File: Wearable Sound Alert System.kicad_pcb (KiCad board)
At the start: 2 copper layers, 87 parts, among them J1 ST-LINK Connector, J8 USB4125-GF-A_REVA2, J9 Extra GPIO Header, SW1 SW_Push, U1 STM32F767ZIT6, U2 TPS63020DSJR, U3 MAX17055ETB+T, U4 2.8_240x320_touch_sd_spi, U6 TPS63020DSJR, U7 BQ21040DBVR

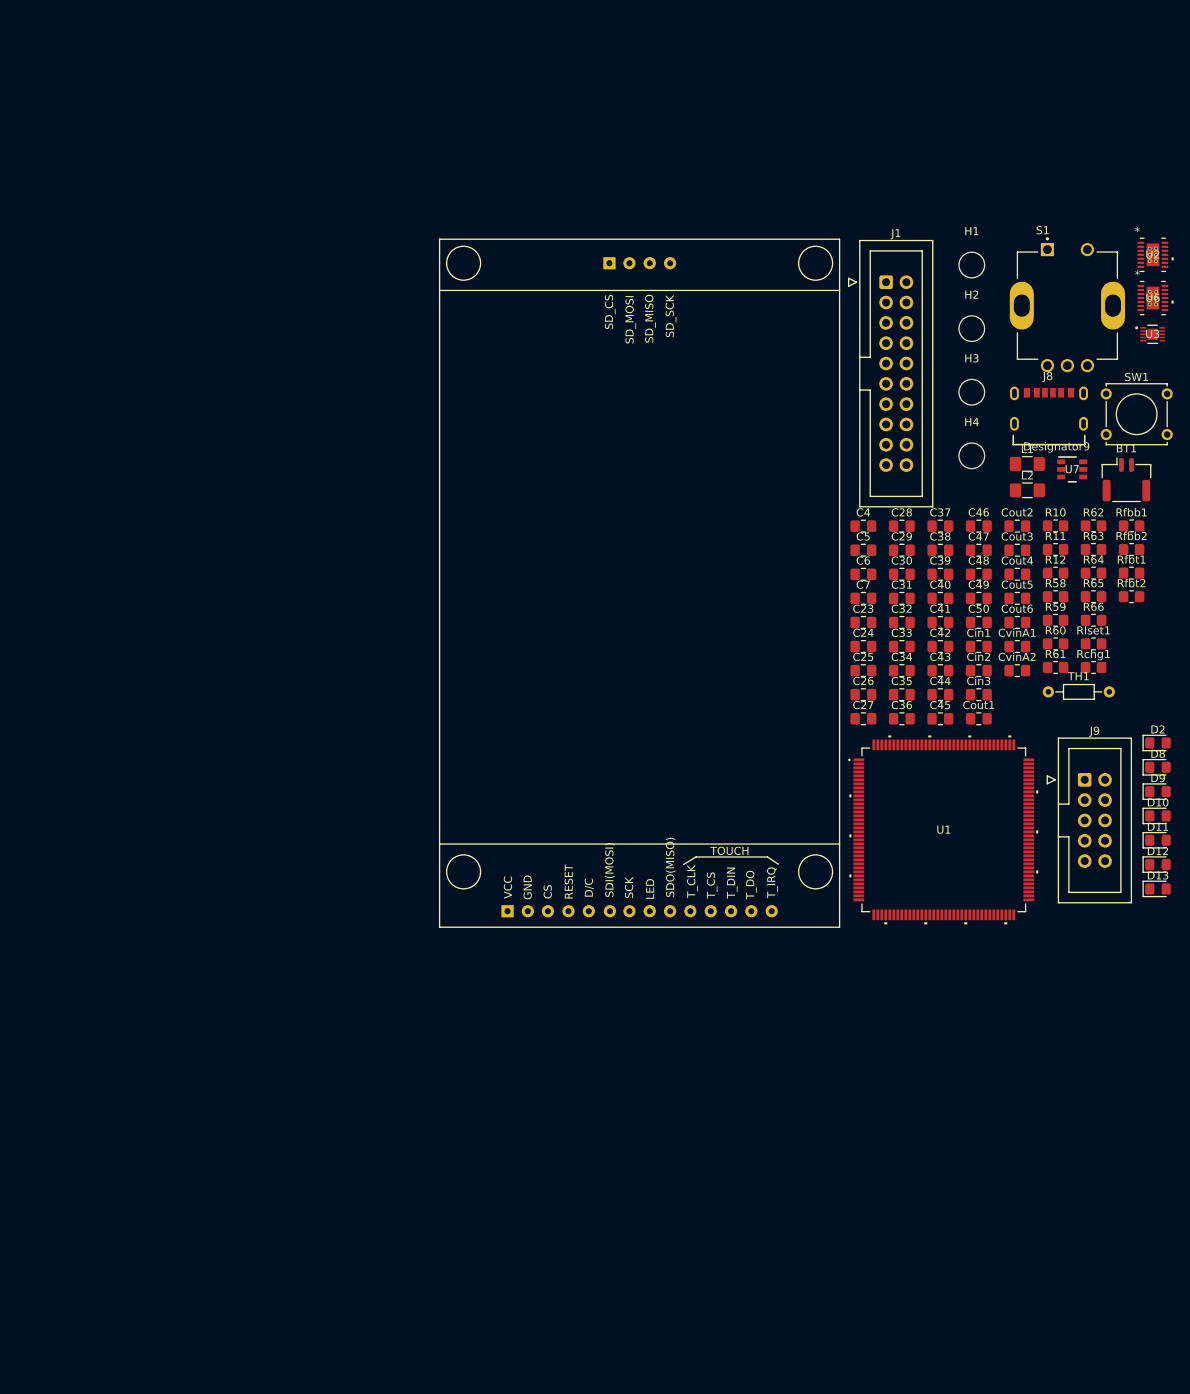
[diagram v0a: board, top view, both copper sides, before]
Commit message: Added updated schematic
Includes BOM, new footprints
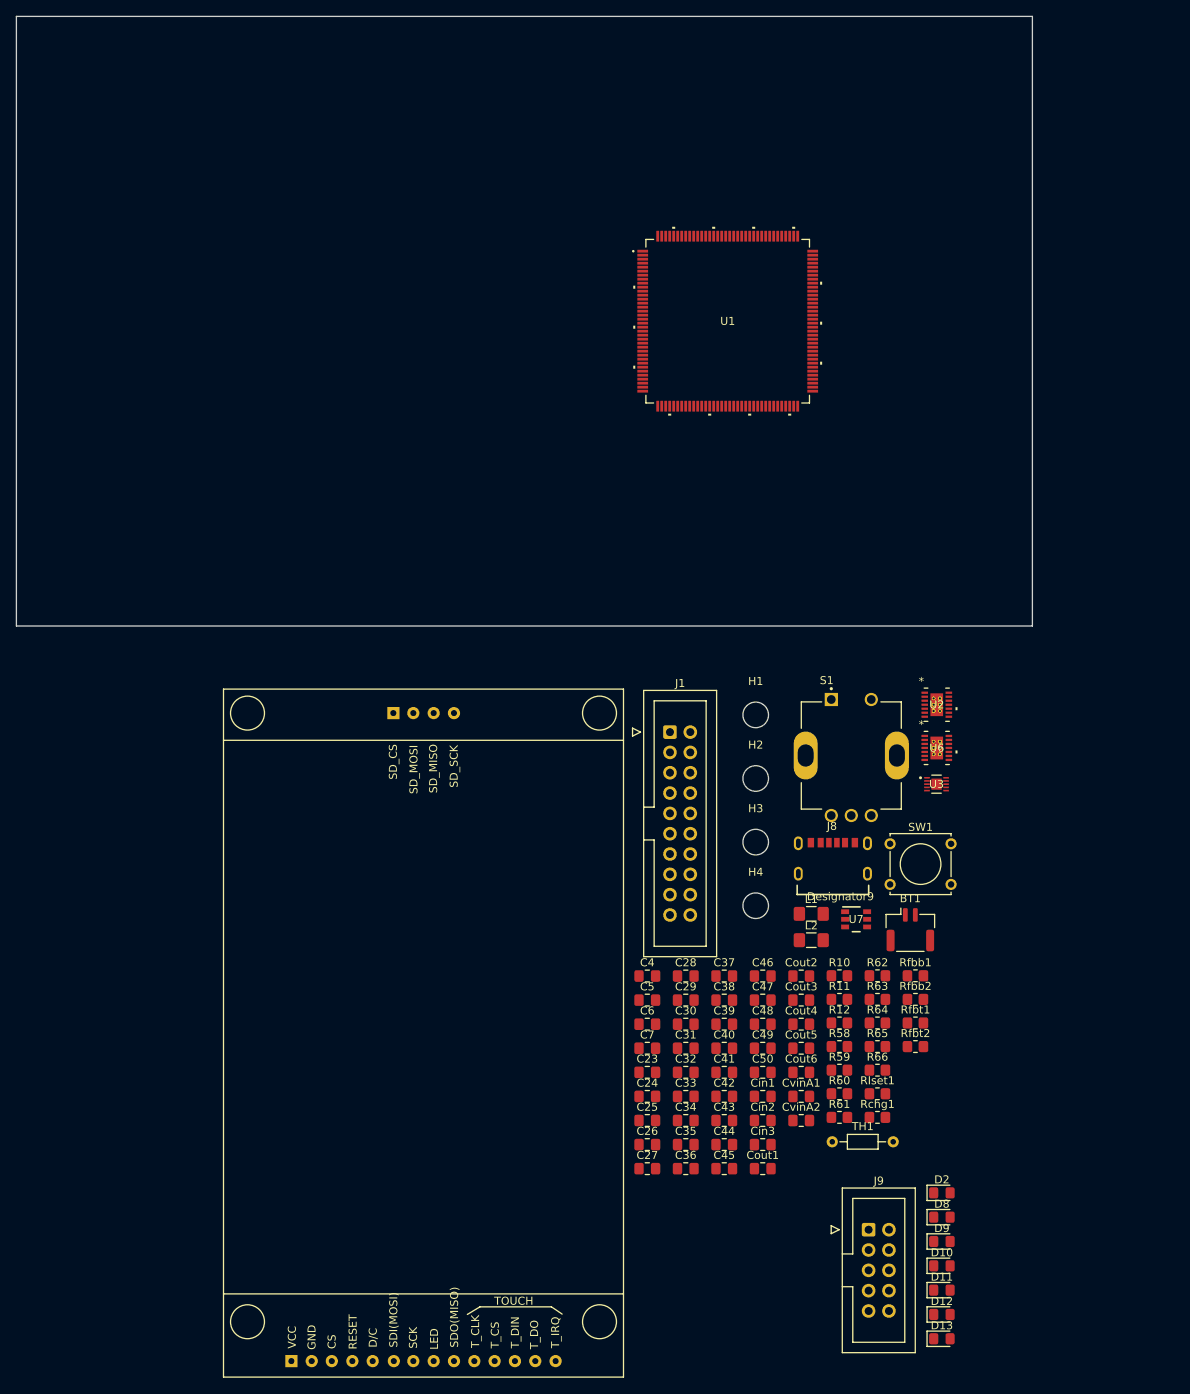
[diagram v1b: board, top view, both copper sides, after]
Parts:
- moved U1 69.1 mm to (114.3, 63.5)
- moved C23 62.4 mm to (104.3, 157.4)
- moved C26 62.4 mm to (104.3, 166.4)
- moved C27 62.4 mm to (104.3, 169.4)
- moved C29 62.4 mm to (109.1, 148.4)
- moved C32 62.4 mm to (109.1, 157.4)
- moved C35 62.4 mm to (109.1, 166.4)
- moved C36 62.4 mm to (109.1, 169.4)
- moved C5 62.4 mm to (104.3, 148.4)
- moved L1 62.4 mm to (124.8, 137.6)
- moved C24 62.4 mm to (104.3, 160.4)
- moved C25 62.4 mm to (104.3, 163.4)
- moved C28 62.4 mm to (109.1, 145.4)
- moved C30 62.4 mm to (109.1, 151.4)
- moved C31 62.4 mm to (109.1, 154.4)
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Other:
- board outline added: 127 x 76.2 mm
